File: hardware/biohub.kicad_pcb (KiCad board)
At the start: 4 copper layers, 89 x 55 mm, 123 parts, among them J1 CONNECTOR, J2 Conn_02x13_Odd_Even, U1 ADUM1412BRWZ, U10 AD8244BRMZ, U11 AD8244BRMZ, U12 TPD4E1B06DCKR, U13 TPD4E1B06DCKR, U2 MCP2210-I_SS, U3 ADUM6020, U4 ADM8660ARZ, U5 ADP7142AUJZ-2.5-R7, U6 ADP7182AUJZ-2.5-R7, U7 ADS1299IPAG, U8 AD8244BRMZ, U9 AD8244BRMZ

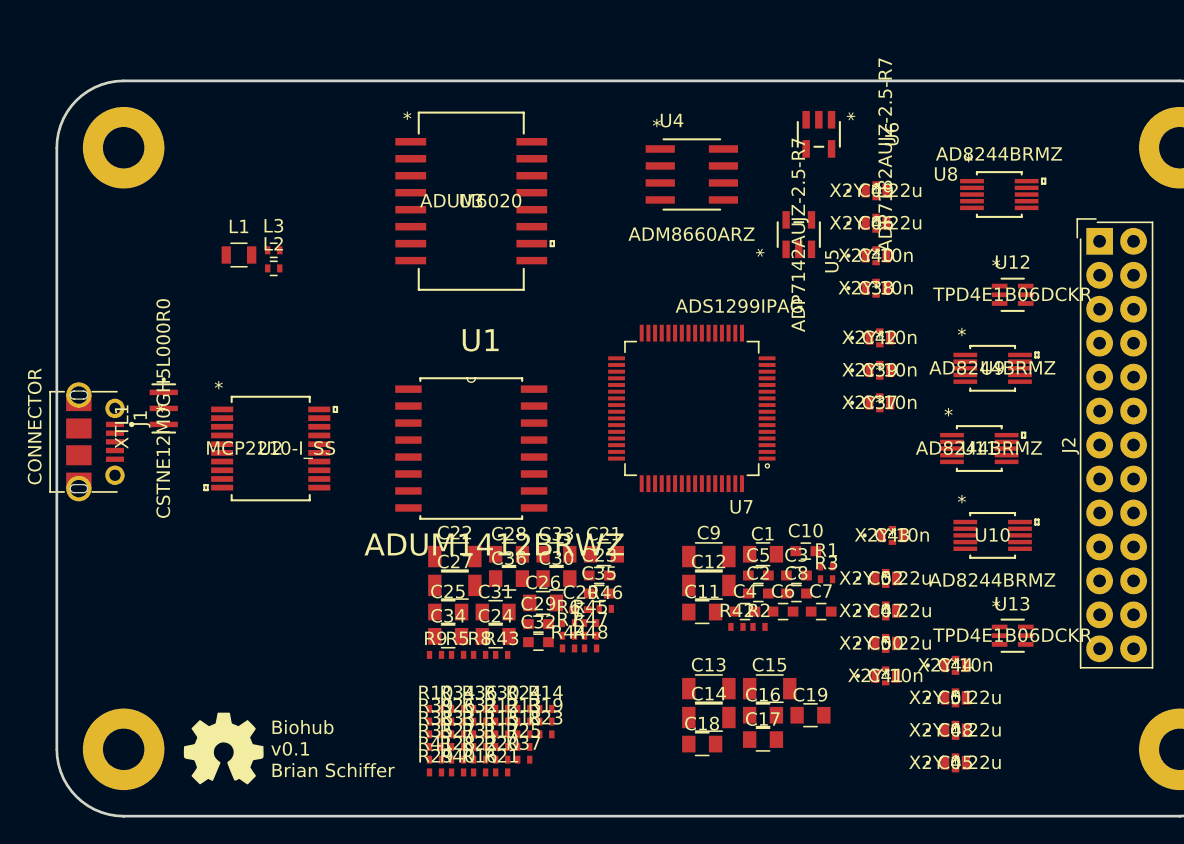
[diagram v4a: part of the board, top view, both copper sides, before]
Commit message: Rough part placement
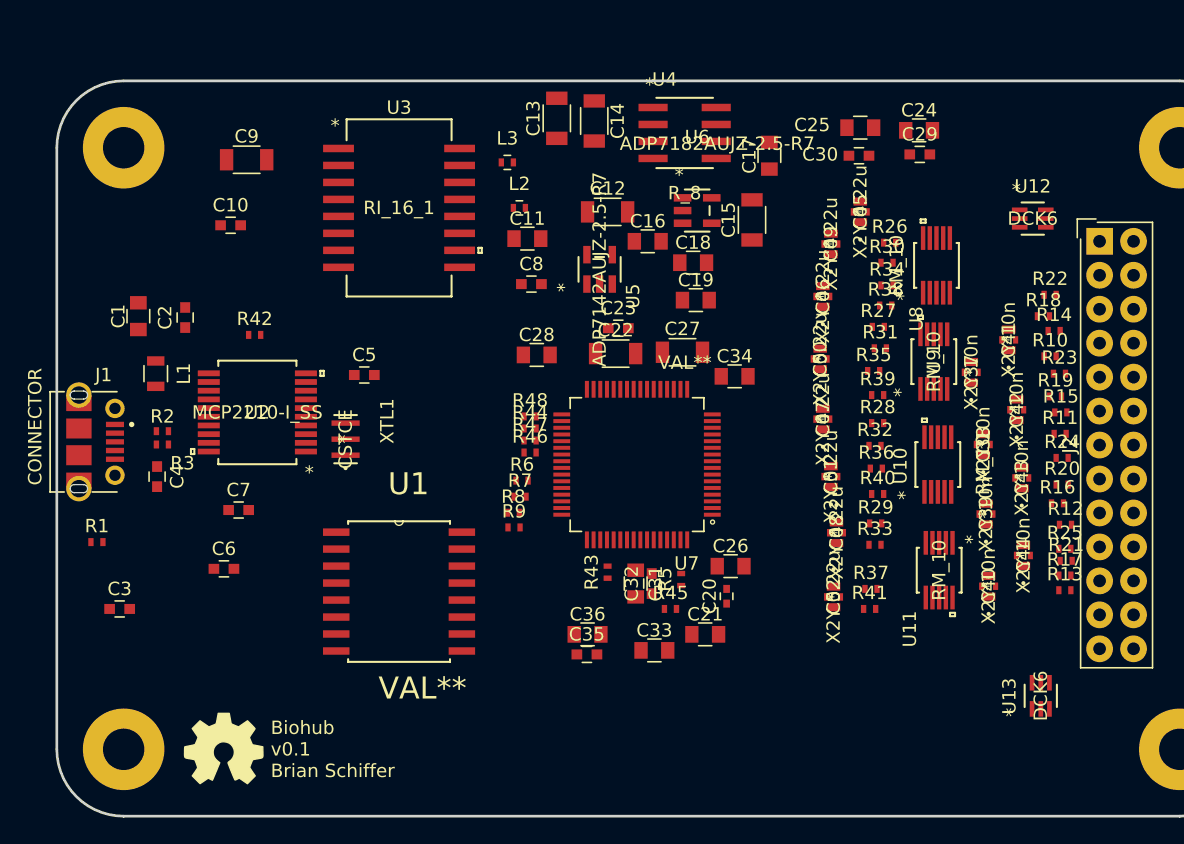
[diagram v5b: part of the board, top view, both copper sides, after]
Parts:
- C30: value 1u -> 0.1u; footprint Capacitors_SMD:C_0805 -> Capacitors_SMD:C_0603
- U1: value ADUM1412BRWZ -> VAL**
- U10, U11, U8, U9: value AD8244BRMZ -> RM_10
- U12, U13: value TPD4E1B06DCKR -> DCK6; footprint TPD4E1B06DCKR -> biohub:TPD4E1B06DCKR
- U3: value ADUM6020 -> RI_16_1
- U4: value ADM8660ARZ -> R_8
- U7: value ADS1299IPAG -> VAL**
- XTL1: value CSTNE12M0GH5L000R0 -> CSTCE
- moved R22 55.0 mm to (178.8, 81.0)
- moved R1 54.6 mm to (107.5, 99.5)
- moved R10 53.0 mm to (178.8, 85.6)
- moved C3 50.7 mm to (109.2, 104.5)
- moved R3 50.7 mm to (112.4, 92.2), turned to 180 degrees
- moved C1 50.0 mm to (110.6, 82.6), turned to 90 degrees
- moved R18 49.9 mm to (178.3, 82.6)
- moved C10 49.4 mm to (117.5, 75.8)
- moved C24 49.4 mm to (169.0, 68.7)
- moved R11 48.9 mm to (179.6, 91.4)
- moved R15 48.3 mm to (179.6, 89.8)
- moved R26 48.3 mm to (166.8, 77.1)
- moved R16 47.7 mm to (179.3, 96.6)
- moved C2 47.6 mm to (114.1, 82.7), turned to 90 degrees
- moved C25 47.6 mm to (164.6, 68.5)
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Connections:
- J2 pad 10: /interface/7P -> /interface/2N
- J2 pad 11: /interface/6N -> /interface/3P
- J2 pad 12: /interface/6P -> /interface/3N
- J2 pad 13: /interface/5N -> /interface/4P
- J2 pad 14: /interface/5P -> /interface/4N
- J2 pad 15: /interface/4N -> /interface/5P
- J2 pad 16: /interface/4P -> /interface/5N
- J2 pad 17: /interface/3N -> /interface/6P
- J2 pad 18: /interface/3P -> /interface/6N
- J2 pad 19: /interface/2N -> /interface/7P
- J2 pad 20: /interface/2P -> /interface/7N
- J2 pad 21: /interface/1N -> /interface/8P
- J2 pad 22: /interface/1P -> /interface/8N
- J2 pad 7: /interface/8N -> /interface/1P
- J2 pad 8: /interface/8P -> /interface/1N
- J2 pad 9: /interface/7N -> /interface/2P

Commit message: Placement cleanup
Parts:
- moved U12 4.73 mm to (178.0, 80.0)
- moved U13 4.32 mm to (177.7, 106.7)
- moved C37 3.50 mm to (176.4, 86.8)
- moved C45 3.00 mm to (165.9, 77.5)
- moved C48 3.00 mm to (164.1, 101.5)
- moved C50 3.00 mm to (162.9, 88.5)
- moved C52 3.00 mm to (163.9, 106.3)
- moved R29 3.00 mm to (167.1, 100.8)
- moved R30 3.00 mm to (167.9, 81.3)
- moved R31 3.00 mm to (167.4, 87.7)
- moved R32 3.00 mm to (167.0, 95.0)
- moved R33 3.00 mm to (167.0, 102.4)
- moved R34 3.00 mm to (167.9, 83.0)
- moved R35 3.00 mm to (166.9, 89.4)
- moved R38 3.00 mm to (167.8, 84.5)
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
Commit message: Near final placement
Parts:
- removed C24, C25: 1u, Capacitors_SMD:C_0805
- added C53: 1u, Capacitors_SMD:C_0805, F.Cu at (155.6, 79.1)
- U1: value VAL** -> **
- U7: value VAL** -> ADS1299
- moved C13 43.2 mm to (151.9, 109.8), turned to 270 degrees
- moved C17 43.0 mm to (156.4, 113.6), turned to 0 degrees
- moved C14 42.1 mm to (141.2, 110.0)
- moved U4 41.4 mm to (146.7, 110.0)
- moved C15 39.6 mm to (148.1, 114.1), turned to 180 degrees
- moved U6 36.2 mm to (156.4, 110.7)
- moved C18 29.5 mm to (156.4, 107.8), turned to 180 degrees
- moved C33 25.5 mm to (155.3, 82.8), turned to 270 degrees
- moved C30 25.0 mm to (142.7, 82.8), turned to 270 degrees
- moved C8 19.3 mm to (137.1, 99.3), turned to 270 degrees
- moved C3 18.5 mm to (112.4, 86.3), turned to 90 degrees
- moved C29 16.9 mm to (157.2, 82.6), turned to 270 degrees
- moved R22 14.6 mm to (175.2, 69.8)
- moved R18 14.3 mm to (175.2, 71.4)
- moved C41 13.9 mm to (173.5, 70.6)
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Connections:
- C49 pad 2: /interface/1N -> /interface/2N
- C51 pad 2: /interface/6P -> /interface/6N
- U12 pad 2: /AFE/BIAS -> Net-(U12-Pad2)
- U12 pad 4: Net-(U12-Pad4) -> /AFE/BIAS
- U13 pad 1: -2V5 -> /AFE/SRB2
- U13 pad 2: /AFE/SRB1 -> Net-(U13-Pad2)
- U13 pad 4: /AFE/SRB2 -> -2V5
- U13 pad 5: Net-(U13-Pad5) -> /AFE/SRB1

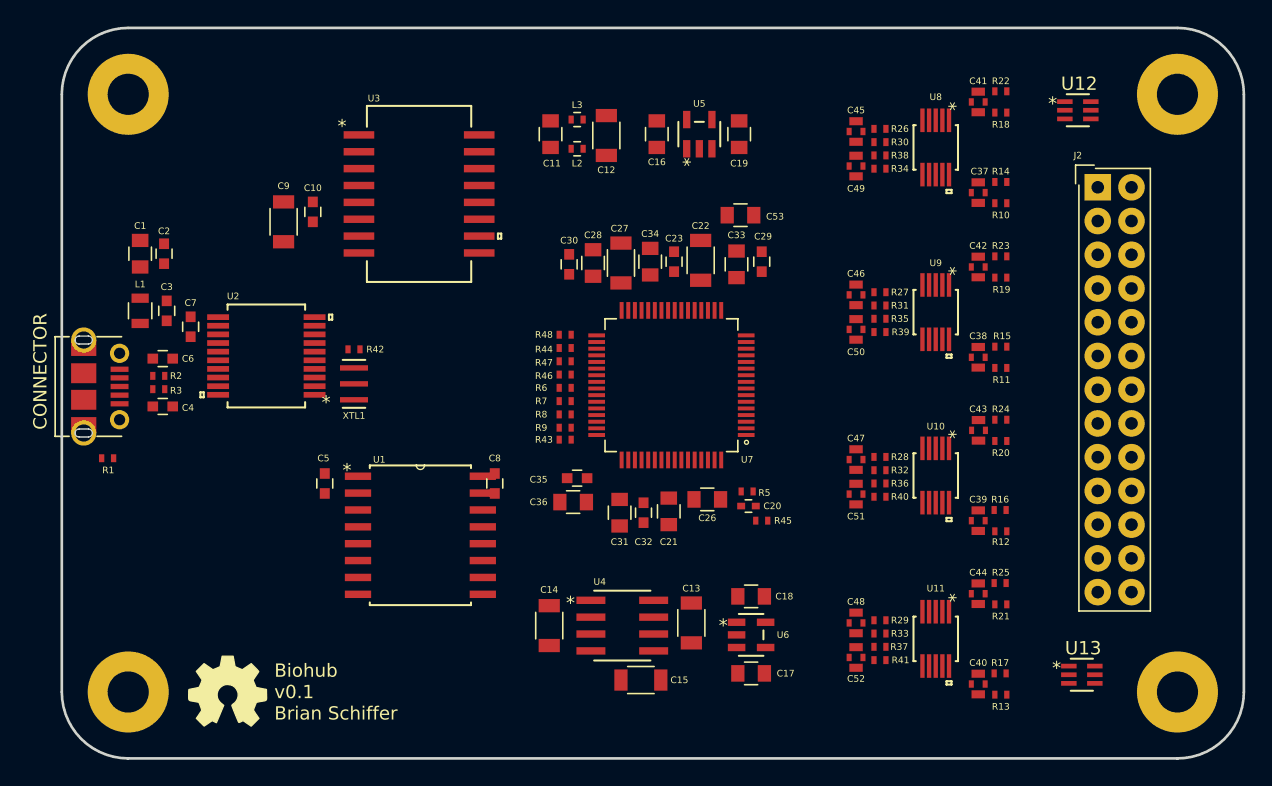
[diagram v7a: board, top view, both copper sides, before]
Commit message: Added Copper Pours
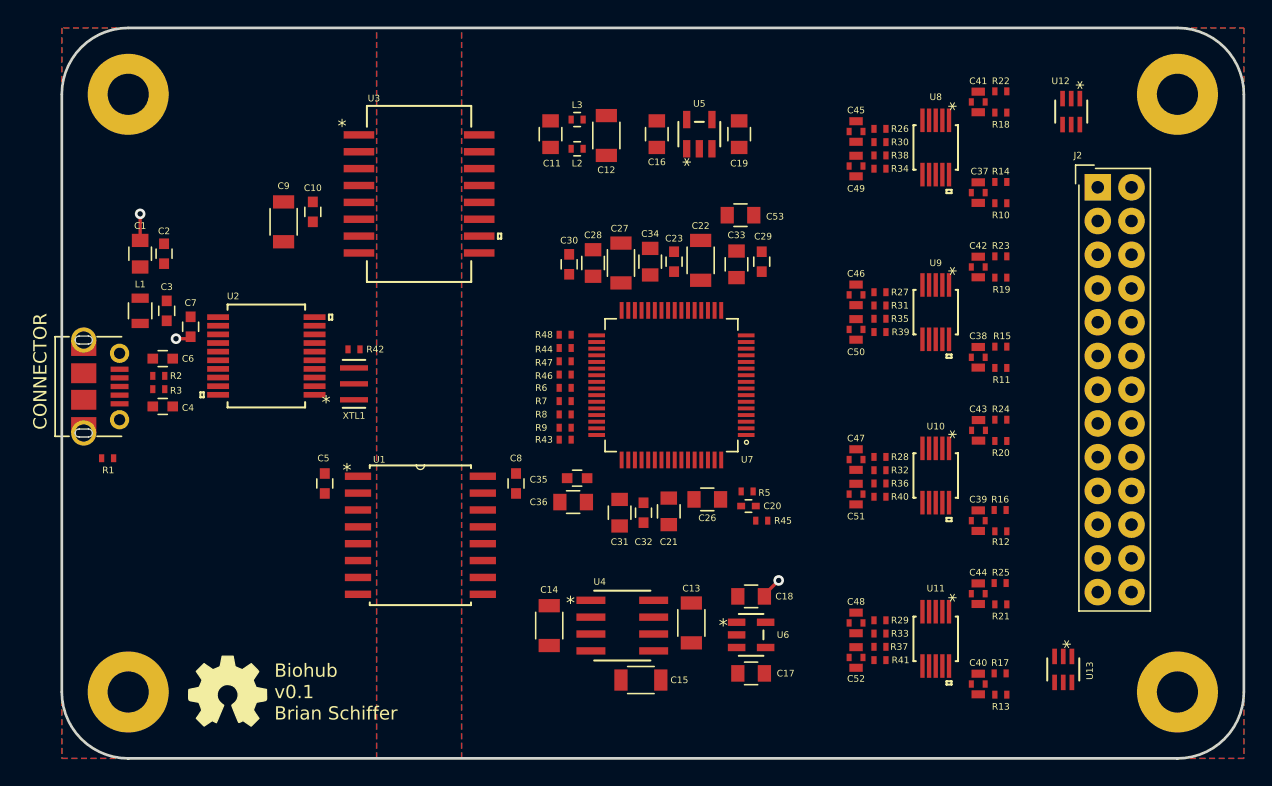
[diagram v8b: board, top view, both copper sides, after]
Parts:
- moved C8 1.60 mm to (138.7, 99.3)
- moved U13 1.46 mm to (179.9, 113.3), turned to 270 degrees
- moved U12 0.51 mm to (180.5, 71.3), turned to 270 degrees
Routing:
- net GNDD: track 0.00 -> 2.00 mm, vias 0 -> 1
- net -2V5: track 0.00 -> 1.65 mm, vias 0 -> 1
- net VCOM: track 0.00 -> 1.16 mm, vias 0 -> 1
- added copper zone on In1.Cu, net +2V5
- added copper zone on In1.Cu, net +3V3
- added copper zone on In2.Cu, net -2V5
- added copper zone on B.Cu, net GND
- added copper zone on F.Cu, net GND
- added copper zone on B.Cu, net GNDD
- added copper zone on F.Cu, net GNDD
- added copper zone on In1.Cu, net VCOM
